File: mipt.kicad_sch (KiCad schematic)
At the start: 3 parts

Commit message: started to do homework 2
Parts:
- added U1: ATmega328-MM, Package_DFN_QFN:QFN-28-1EP_4x4mm_P0.45mm_EP2.4x2.4mm, symbol MCU_Microchip_ATmega:ATmega328-MM
- added U3: ~, symbol homework:AW9523B
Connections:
- new net: U1.18 (GND), U1.29 (GND), U1.4 (GND)
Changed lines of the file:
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@@
+	)
+	(symbol
+		(lib_id "homework:AW9523B")
+		(at 96.52 116.84 0)
+		(unit 1)
+		(exclude_from_sim no)
+		(in_bom yes)
+		(on_board yes)
+		(dnp no)
+		(fields_autoplaced yes)
+		(property "Reference" "U3"
+			(at 105.41 105.41 0)
+			(effects
+				(font
+					(size 1.27 1.27)
+				)
+			)
+		)
+		(property "Value" "~"
+			(at 105.41 107.95 0)
+			(effects
+				(font
+					(size 1.27 1.27)
+				)
+			)
+		)
+		(property "Footprint" ""
+			(at 96.52 118.11 0)
+			(effects
+				(font
+					(size 1.27 1.27)
+				)
+				(hide yes)
+			)
+		)
+		(property "Datasheet" ""
+			(at 96.52 118.11 0)
+			(effects
+				(font
+					(size 1.27 1.27)
+				)
+				(hide yes)
+			)
+		)
+		(property "Description" ""
+			(at 96.52 118.11 0)
+			(effects
+				(font
+					(size 1.27 1.27)
+				)
+				(hide yes)
+			)
+		)
+		(pin ""
+		)
+		(pin ""
+		)
+		(pin ""
+		)
+		(instances
+			(project ""
+				(path "/34d483ea-61c1-4e08-b30a-5dee616d4777"
+					(reference "U3")
+					(unit 1)
+				)
+			)
+		)
 	)
 	(symbol
@@
 					(unit 1)
 				)
+			)
+		)
+	)
+	(symbol
+		(lib_id "MCU_Microchip_ATmega:ATmega328-MM")
+		(at 72.39 111.76 0)
+		(unit 1)
+		(exclude_from_sim no)
+		(in_bom yes)
+		(on_board yes)
+		(dnp no)
+		(fields_autoplaced yes)
+		(property "Reference" "U1"
+			(at 50.8 74.9614 0)
+			(effects
+				(font
+					(size 1.27 1.27)
+				)
+			)
+		)
+		(property "Value" "ATmega328-MM"
+			(at 50.8 77.5014 0)
+			(effects
+				(font
+					(size 1.27 1.27)
+				)
+			)
+		)
+		(property "Footprint" "Package_DFN_QFN:QFN-28-1EP_4x4mm_P0.45mm_EP2.4x2.4mm"
+			(at 72.39 111.76 0)
+			(effects
+				(font
+					(size 1.27 1.27)
+					(italic yes)
+				)
+				(hide yes)
+			)
+		)
+		(property "Datasheet" "http://ww1.microchip.com/downloads/en/DeviceDoc/ATmega328_P%20AVR%20MCU%20with%20picoPower%20Technology%20Data%20Sheet%2040001984A.pdf"
+			(at 72.39 111.76 0)
+			(effects
+				(font
+					(size 1.27 1.27)
+				)
+				(hide yes)
+			)
+		)
+		(property "Description" "20MHz, 32kB Flash, 2kB SRAM, 1kB EEPROM, QFN-28"
+			(at 72.39 111.76 0)
+			(effects
+				(font
+					(size 1.27 1.27)
+				)
+				(hide yes)
+			)
+		)
+		(pin "1"
+		)
+		(pin "27"
+		)
+		(pin "28"
+		)
+		(pin "29"
+		)
+		(pin "3"
+		)
+		(pin "4"
+		)
+		(pin "5"
+		)
+		(pin "6"
+		)
+		(pin "7"
+		)
+		(pin "8"
+		)
+		(pin "9"
+		)
+		(pin "10"
+		)
+		(pin "11"
+		)
+		(pin "12"
+		)
+		(pin "13"
+		)
+		(pin "14"
+		)
+		(pin "15"
+		)
+		(pin "16"
+		)
+		(pin "17"
+		)
+		(pin "18"
+		)
+		(pin "19"
+		)
+		(pin "2"
+		)
+		(pin "20"
+		)
+		(pin "21"
+		)
+		(pin "22"
+		)
+		(pin "23"
+		)
+		(pin "24"
+		)
+		(pin "25"
+		)
+		(pin "26"
+		)
+		(instances
+			(project ""
+				(path "/34d483ea-61c1-4e08-b30a-5dee616d4777"
+					(reference "U1")
+					(unit 1)
+				)

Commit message: update basic schema
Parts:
- removed BT1: 3V, Battery:BatteryHolder_Keystone_1058_1x2032, symbol Device:Battery_Cell
- removed D1: red, LED_THT:LED_D5.0mm, symbol Device:LED
- removed R1: 1k, Resistor_THT:R_Axial_DIN0309_L9.0mm_D3.2mm_P12.70mm_Horizontal, symbol Device:R
- removed U1: ATmega328-MM, Package_DFN_QFN:QFN-28-1EP_4x4mm_P0.45mm_EP2.4x2.4mm, symbol MCU_Microchip_ATmega:ATmega328-MM
- removed U3: ~, symbol homework:AW9523B
- added U2: AW9523B, MODULE, symbol mipt:AW9523B
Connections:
- no-connect marks 0 -> 24

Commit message: update schemas
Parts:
- U2: footprint MODULE -> mipt:TQFN-24-1EP_4x4mm_P0.5mm_EP2.1x2.1mm
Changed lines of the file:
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@@
 			)
 		)
-		(property "Footprint" "MODULE"
+		(property "Footprint" "mipt:TQFN-24-1EP_4x4mm_P0.5mm_EP2.1x2.1mm"
 			(at 53.34 58.42 0)
 			(effects

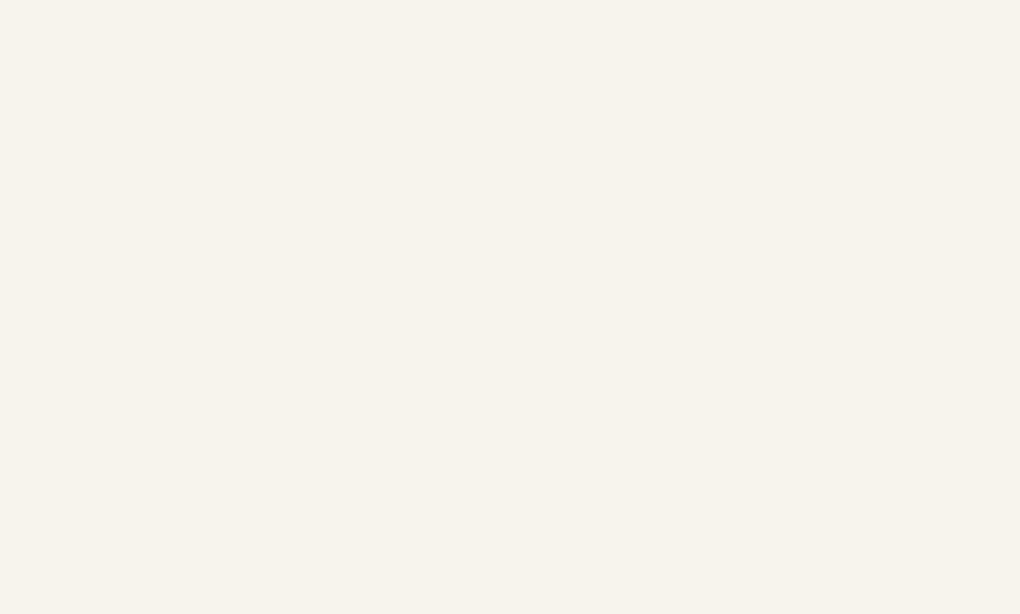
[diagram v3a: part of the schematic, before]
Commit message: update HLK-7628N
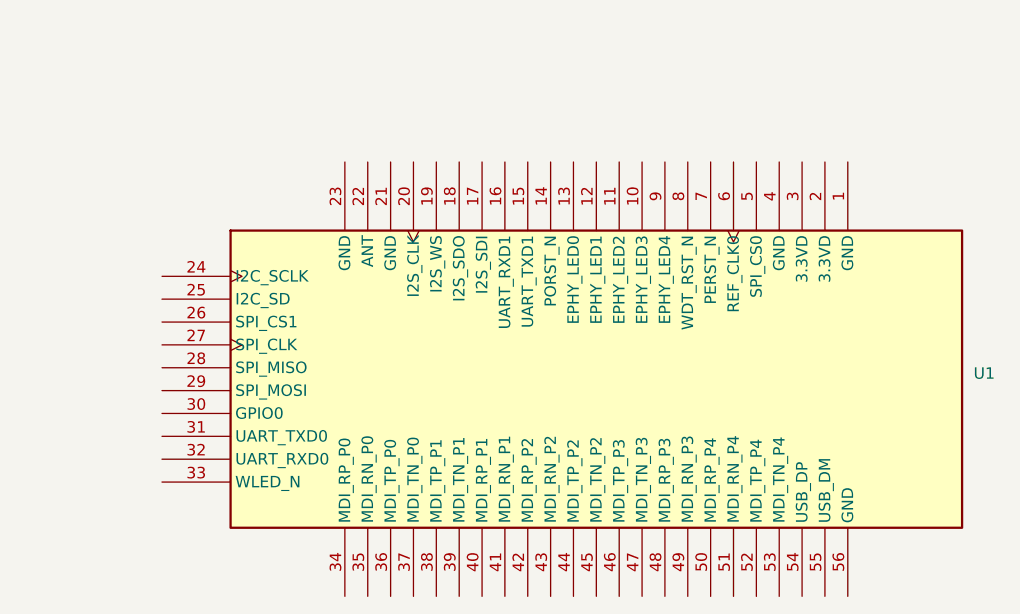
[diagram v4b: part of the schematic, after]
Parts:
- added U1: ~, mipt:HLK-7628N, symbol mipt:HLK-7628N
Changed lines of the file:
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@@
+	)
+	(symbol
+		(lib_id "mipt:HLK-7628N")
+		(at 160.02 80.01 0)
+		(unit 1)
+		(exclude_from_sim no)
+		(in_bom yes)
+		(on_board yes)
+		(dnp no)
+		(fields_autoplaced yes)
+		(property "Reference" "U1"
+			(at 201.93 79.3749 0)
+			(effects
+				(font
+					(size 1.27 1.27)
+				)
+				(justify left)
+			)
+		)
+		(property "Value" "~"
+			(at 201.93 81.28 0)
+			(effects
+				(font
+					(size 1.27 1.27)
+				)
+				(justify left)
+			)
+		)
+		(property "Footprint" "mipt:HLK-7628N"
+			(at 160.02 80.01 0)
+			(effects
+				(font
+					(size 1.27 1.27)
+				)
+				(hide yes)
+			)
+		)
+		(property "Datasheet" "./datasheets/HLK-7628N_V2.6.pdf"
+			(at 160.02 80.01 0)
+			(effects
+				(font
+					(size 1.27 1.27)
+				)
+				(hide yes)
+			)
+		)
+		(property "Description" ""
+			(at 160.02 80.01 0)
+			(effects
+				(font
+					(size 1.27 1.27)
+				)
+				(hide yes)
+			)
+		)
+		(pin "8"
+		)
+		(pin "9"
+		)
+		(pin "14"
+		)
+		(pin "50"
+		)
+		(pin "56"
+		)
+		(pin "49"
+		)
+		(pin "52"
+		)
+		(pin "37"
+		)
+		(pin "6"
+		)
+		(pin "53"
+		)
+		(pin "40"
+		)
+		(pin "22"
+		)
+		(pin "45"
+		)
+		(pin "18"
+		)
+		(pin "34"
+		)
+		(pin "21"
+		)
+		(pin "24"
+		)
+		(pin "28"
+		)
+		(pin "35"
+		)
+		(pin "23"
+		)
+		(pin "43"
+		)
+		(pin "29"
+		)
+		(pin "3"
+		)
+		(pin "39"
+		)
+		(pin "15"
+		)
+		(pin "30"
+		)
+		(pin "1"
+		)
+		(pin "11"
+		)
+		(pin "20"
+		)
+		(pin "19"
+		)
+		(pin "33"
+		)
+		(pin "2"
+		)
+		(pin "32"
+		)
+		(pin "38"
+		)
+		(pin "41"
+		)
+		(pin "51"
+		)
+		(pin "27"
+		)
+		(pin "10"
+		)
+		(pin "54"
+		)
+		(pin "55"
+		)
+		(pin "4"
+		)
+		(pin "26"
+		)
+		(pin "42"
+		)
+		(pin "25"
+		)
+		(pin "31"
+		)
+		(pin "12"
+		)
+		(pin "44"
+		)
+		(pin "13"
+		)
+		(pin "5"
+		)
+		(pin "7"
+		)
+		(pin "47"
+		)
+		(pin "36"
+		)
+		(pin "48"
+		)
+		(pin "16"
+		)
+		(pin "46"
+		)
+		(pin "17"
+		)
+		(instances
+			(project ""
+				(path "/34d483ea-61c1-4e08-b30a-5dee616d4777"
+					(reference "U1")
+					(unit 1)
+				)
+			)
+		)
 	)
 	(symbol

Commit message: update BL0910
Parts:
- added U3: XS2184, symbol mipt:XS2184
- added U4: BL0910, Package_QFP:LQFP-48_7x7mm_P0.5mm, symbol mipt:bl0910
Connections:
- new net: U3.1 (N.C.), U3.15 (N.C.), U3.16 (N.C.), U3.17 (N.C.), U3.19 (N.C.), U3.20 (N.C.), U3.24 (N.C.), U3.38 (N.C.), U3.42 (N.C.), U3.43 (N.C.), U3.44 (N.C.), U3.46 (N.C.)
- new net: U3.25 (DRAIN4), U3.26 (DRAIN4)
- new net: U3.29 (DRAIN3), U3.30 (DRAIN3)
- new net: U3.36 (DRAIN1), U3.39 (DRAIN1)
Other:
- moved on the sheet: U1

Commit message: some fixes
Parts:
- U1: value ~ -> HLK-7628N
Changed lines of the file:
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@@
+	)
+	(symbol
+		(lib_id "mipt:HLK-7628N")
+		(at 156.21 55.88 0)
+		(unit 1)
+		(exclude_from_sim no)
+		(in_bom yes)
+		(on_board yes)
+		(dnp no)
+		(fields_autoplaced yes)
+		(property "Reference" "U1"
+			(at 198.12 54.6099 0)
+			(effects
+				(font
+					(size 1.27 1.27)
+				)
+				(justify left)
+			)
+		)
+		(property "Value" "HLK-7628N"
+			(at 198.12 57.1499 0)
+			(effects
+				(font
+					(size 1.27 1.27)
+				)
+				(justify left)
+			)
+		)
+		(property "Footprint" "mipt:HLK-7628N"
+			(at 156.21 55.88 0)
+			(effects
+				(font
+					(size 1.27 1.27)
+				)
+				(hide yes)
+			)
+		)
+		(property "Datasheet" "./datasheets/HLK-7628N_V2.6.pdf"
+			(at 156.21 55.88 0)
+			(effects
+				(font
+					(size 1.27 1.27)
+				)
+				(hide yes)
+			)
+		)
+		(property "Description" ""
+			(at 156.21 55.88 0)
+			(effects
+				(font
+					(size 1.27 1.27)
+				)
+				(hide yes)
+			)
+		)
+		(pin "20"
+		)
+		(pin "31"
+		)
+		(pin "32"
+		)
+		(pin "23"
+		)
+		(pin "55"
+		)
+		(pin "56"
+		)
+		(pin "30"
+		)
+		(pin "35"
+		)
+		(pin "36"
+		)
+		(pin "17"
+		)
+		(pin "18"
+		)
+		(pin "12"
+		)
+		(pin "11"
+		)
+		(pin "13"
+		)
+		(pin "14"
+		)
+		(pin "15"
+		)
+		(pin "16"
+		)
+		(pin "48"
+		)
+		(pin "49"
+		)
+		(pin "46"
+		)
+		(pin "47"
+		)
+		(pin "39"
+		)
+		(pin "4"
+		)
+		(pin "26"
+		)
+		(pin "8"
+		)
+		(pin "9"
+		)
+		(pin "40"
+		)
+		(pin "41"
+		)
+		(pin "10"
+		)
+		(pin "6"
+		)
+		(pin "7"
+		)
+		(pin "1"
+		)
+		(pin "2"
+		)
+		(pin "44"
+		)
+		(pin "45"
+		)
+		(pin "42"
+		)
+		(pin "43"
+		)
+		(pin "29"
+		)
+		(pin "51"
+		)
+		(pin "52"
+		)
+		(pin "27"
+		)
+		(pin "37"
+		)
+		(pin "38"
+		)
+		(pin "25"
+		)
+		(pin "28"
+		)
+		(pin "53"
+		)
+		(pin "54"
+		)
+		(pin "24"
+		)
+		(pin "3"
+		)
+		(pin "5"
+		)
+		(pin "50"
+		)
+		(pin "33"
+		)
+		(pin "34"
+		)
+		(pin "21"
+		)
+		(pin "22"
+		)
+		(pin "19"
+		)
+		(instances
+			(project ""
+				(path "/34d483ea-61c1-4e08-b30a-5dee616d4777"
+					(reference "U1")
+					(unit 1)
+				)
+			)
+		)
 	)
 	(symbol
@@
 					(unit 1)
 				)
-			)
-		)
-	)
-	(symbol
-		(lib_id "mipt:HLK-7628N")
-		(at 142.24 57.15 0)
-		(unit 1)
-		(exclude_from_sim no)
-		(in_bom yes)
-		(on_board yes)
-		(dnp no)
-		(fields_autoplaced yes)
-		(property "Reference" "U1"
-			(at 184.15 56.5149 0)
-			(effects
-				(font
-					(size 1.27 1.27)
-				)
-				(justify left)
-			)
-		)
-		(property "Value" "~"
-			(at 184.15 58.42 0)
-			(effects
-				(font
-					(size 1.27 1.27)
-				)
-				(justify left)
-			)
-		)
-		(property "Footprint" "mipt:HLK-7628N"
-			(at 142.24 57.15 0)
-			(effects
-				(font
-					(size 1.27 1.27)
-				)
-				(hide yes)
-			)
-		)
-		(property "Datasheet" "./datasheets/HLK-7628N_V2.6.pdf"
-			(at 142.24 57.15 0)
-			(effects
-				(font
-					(size 1.27 1.27)
-				)
-				(hide yes)
-			)
-		)
-		(property "Description" ""
-			(at 142.24 57.15 0)
-			(effects
-				(font
-					(size 1.27 1.27)
-				)
-				(hide yes)
-			)
-		)
-		(pin "8"
-		)
-		(pin "9"
-		)
-		(pin "14"
-		)
-		(pin "50"
-		)
-		(pin "56"
-		)
-		(pin "49"
-		)
-		(pin "52"
-		)
-		(pin "37"
-		)
-		(pin "6"
-		)
-		(pin "53"
-		)
-		(pin "40"
-		)
-		(pin "22"
-		)
-		(pin "45"
-		)
-		(pin "18"
-		)
-		(pin "34"
-		)
-		(pin "21"
-		)
-		(pin "24"
-		)
-		(pin "28"
-		)
-		(pin "35"
-		)
-		(pin "23"
-		)
-		(pin "43"
-		)
-		(pin "29"
-		)
-		(pin "3"
-		)
-		(pin "39"
-		)
-		(pin "15"
-		)
-		(pin "30"
-		)
-		(pin "1"
-		)
-		(pin "11"
-		)
-		(pin "20"
-		)
-		(pin "19"
-		)
-		(pin "33"
-		)
-		(pin "2"
-		)
-		(pin "32"
-		)
-		(pin "38"
-		)
-		(pin "41"
-		)
-		(pin "51"
-		)
-		(pin "27"
-		)
-		(pin "10"
-		)
-		(pin "54"
-		)
-		(pin "55"
-		)
-		(pin "4"
-		)
-		(pin "26"
-		)
-		(pin "42"
-		)
-		(pin "25"
-		)
-		(pin "31"
-		)
-		(pin "12"
-		)
-		(pin "44"
-		)
-		(pin "13"
-		)
-		(pin "5"
-		)
-		(pin "7"
-		)
-		(pin "47"
-		)
-		(pin "36"
-		)
-		(pin "48"
-		)
-		(pin "16"
-		)
-		(pin "46"
-		)
-		(pin "17"
-		)
-		(instances
-			(project ""
-				(path "/34d483ea-61c1-4e08-b30a-5dee616d4777"
-					(reference "U1")
-					(unit 1)
-				)

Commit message: cleanup and reorganisation of project
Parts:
- removed U1: HLK-7628N, mipt:HLK-7628N, symbol mipt:HLK-7628N
- removed U2: AW9523B, mipt:TQFN-24-1EP_4x4mm_P0.5mm_EP2.1x2.1mm, symbol mipt:AW9523B
- removed U3: XS2184, symbol mipt:XS2184
- removed U4: BL0910, Package_QFP:LQFP-48_7x7mm_P0.5mm, symbol mipt:bl0910
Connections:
- no-connect marks 24 -> 0
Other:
- added sheet home work 2 (home work 2.kicad_sch)
- added sheet home work 3 (home work 3.kicad_sch)

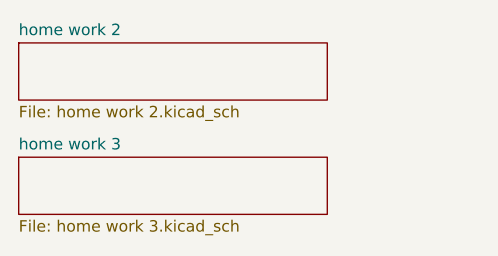
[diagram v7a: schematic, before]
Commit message: update schemas structure
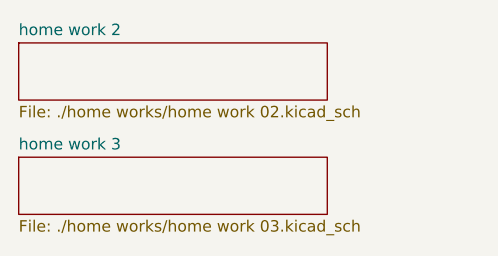
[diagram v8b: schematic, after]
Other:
- sheet home work 2: file home work 2.kicad_sch -> ./home works/home work 02.kicad_sch
- sheet home work 3: file home work 3.kicad_sch -> ./home works/home work 03.kicad_sch
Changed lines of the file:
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@@
 			)
 		)
-		(property "Sheetfile" "home work 2.kicad_sch"
+		(property "Sheetfile" "./home works/home work 02.kicad_sch"
 			(at 17.78 25.9846 0)
 			(effects
@@
 			)
 		)
-		(property "Sheetfile" "home work 3.kicad_sch"
+		(property "Sheetfile" "./home works/home work 03.kicad_sch"
 			(at 17.78 38.6846 0)
 			(effects
